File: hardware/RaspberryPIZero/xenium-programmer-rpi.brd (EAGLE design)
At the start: 99.1 x 78.7 mm, 21 parts, among them P1 B3F-1052, P2 B3F-1052, P3 B3F-1052, P4 B3F-1052

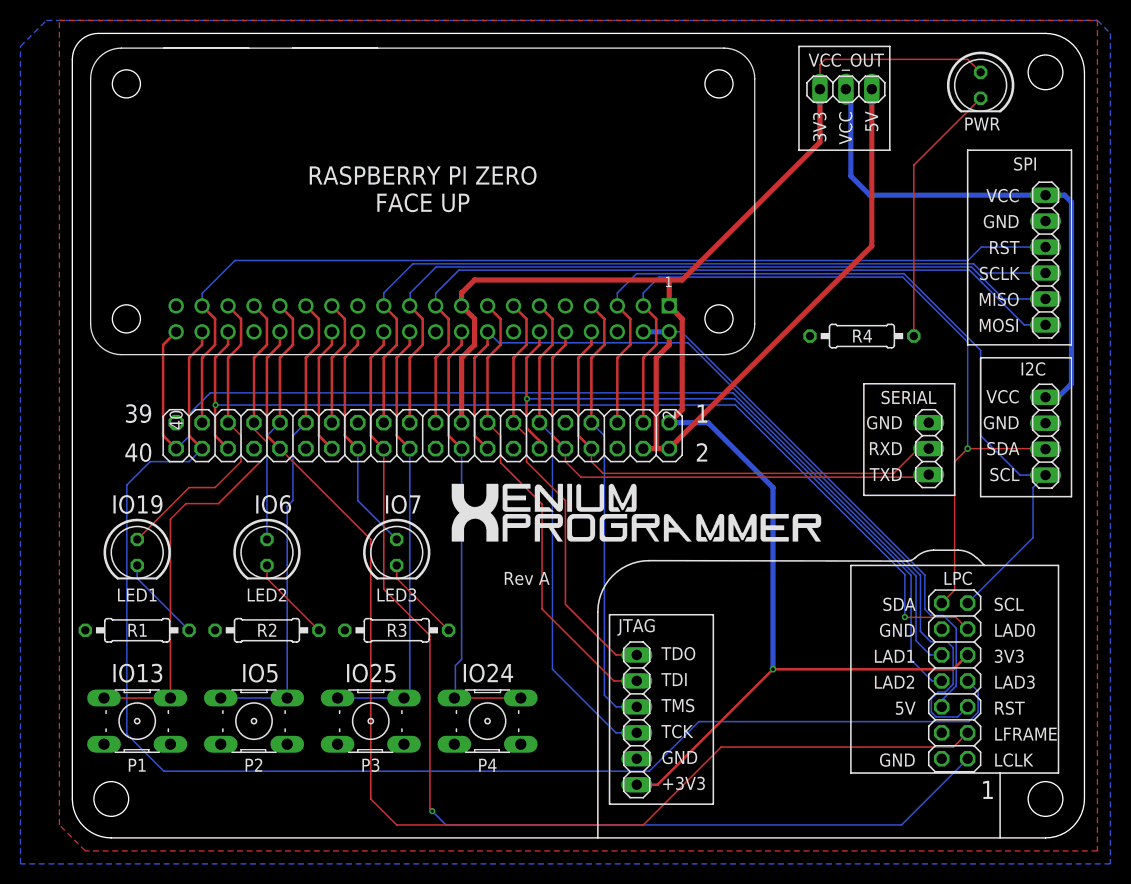
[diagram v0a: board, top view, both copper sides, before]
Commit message: Added C1 on RPI PCB to prevent brownout caused by OX LED sometimes, added jumper to control +3v3 for OX chips. Moved RPI PCB to Rev B
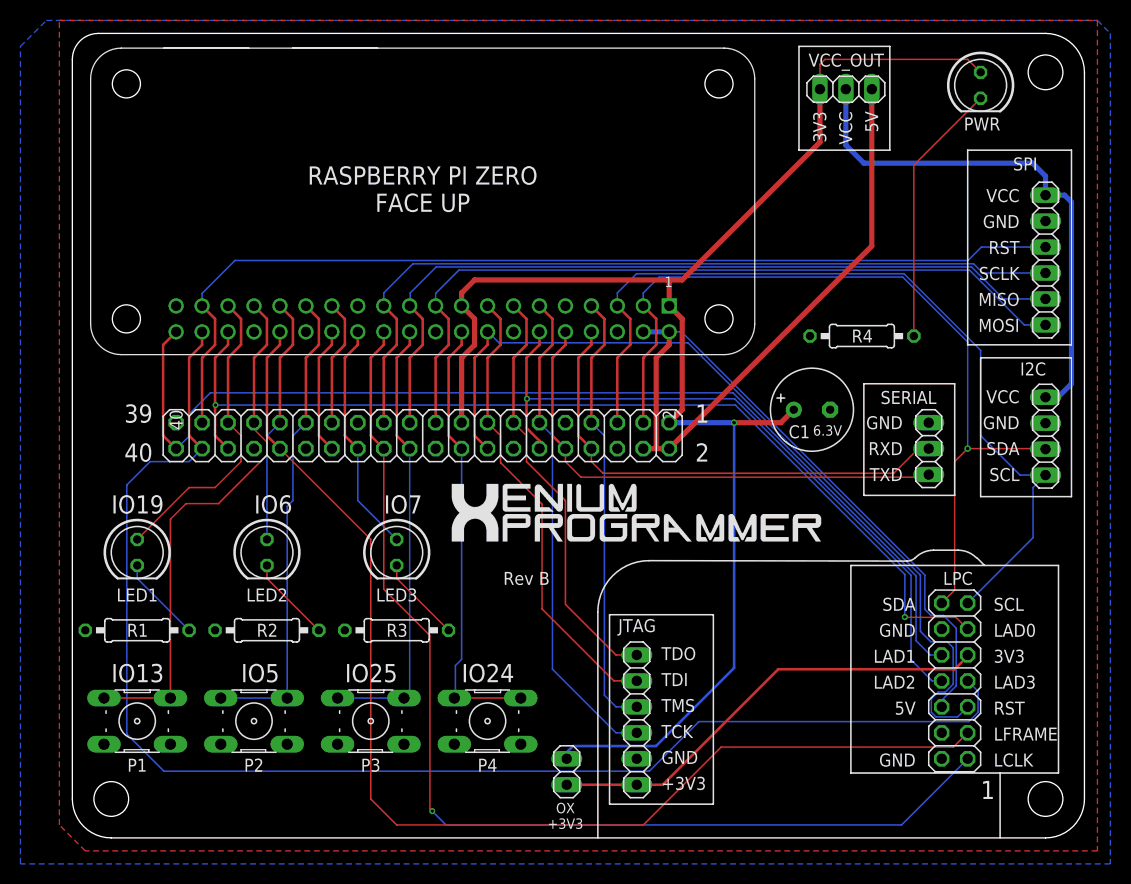
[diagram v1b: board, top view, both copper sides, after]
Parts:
- added C1: 150µF, rcl:E3,5-8
- added JP1: (no value), pinhead:1X02
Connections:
- new net N$6: JP1.2, JTAG.1, LPC.9
- net +3V3: now also C1.+, JP1.1; no longer JTAG.1, LPC.9
- net GND: now also C1.-
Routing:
- net N$6: track 0.00 -> 44.6 mm
- net +3V3: track 162.2 -> 151.2 mm
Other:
- board text added: "6.3V"
- board text added: "OX +3V3"
- board text added: "Rev B"
- board text removed: "Rev A"
